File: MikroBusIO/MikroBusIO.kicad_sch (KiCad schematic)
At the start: 0 parts

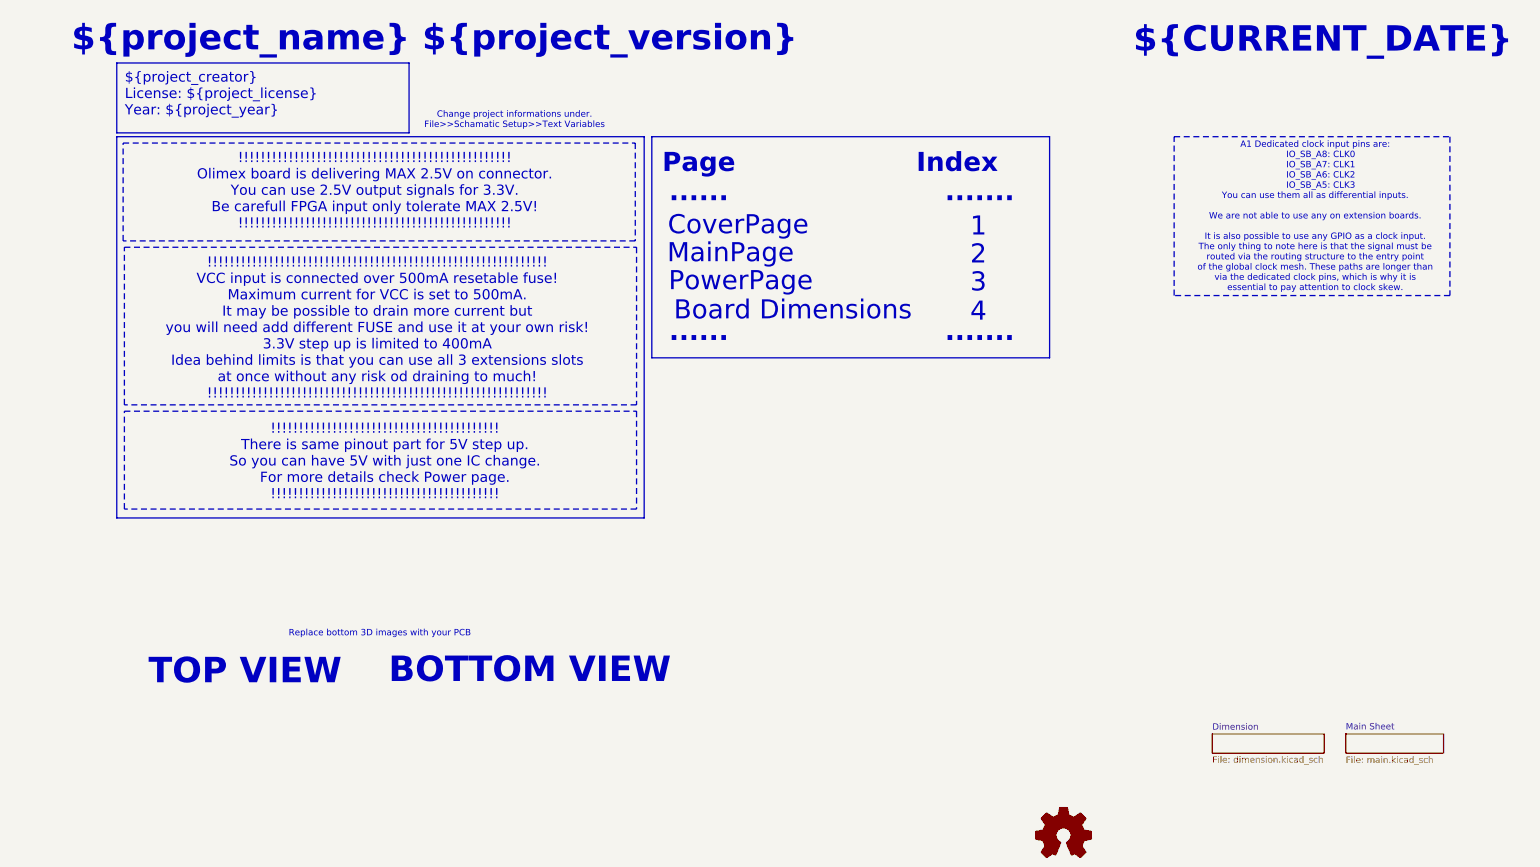
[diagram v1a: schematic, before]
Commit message: Cleanup MikroBus
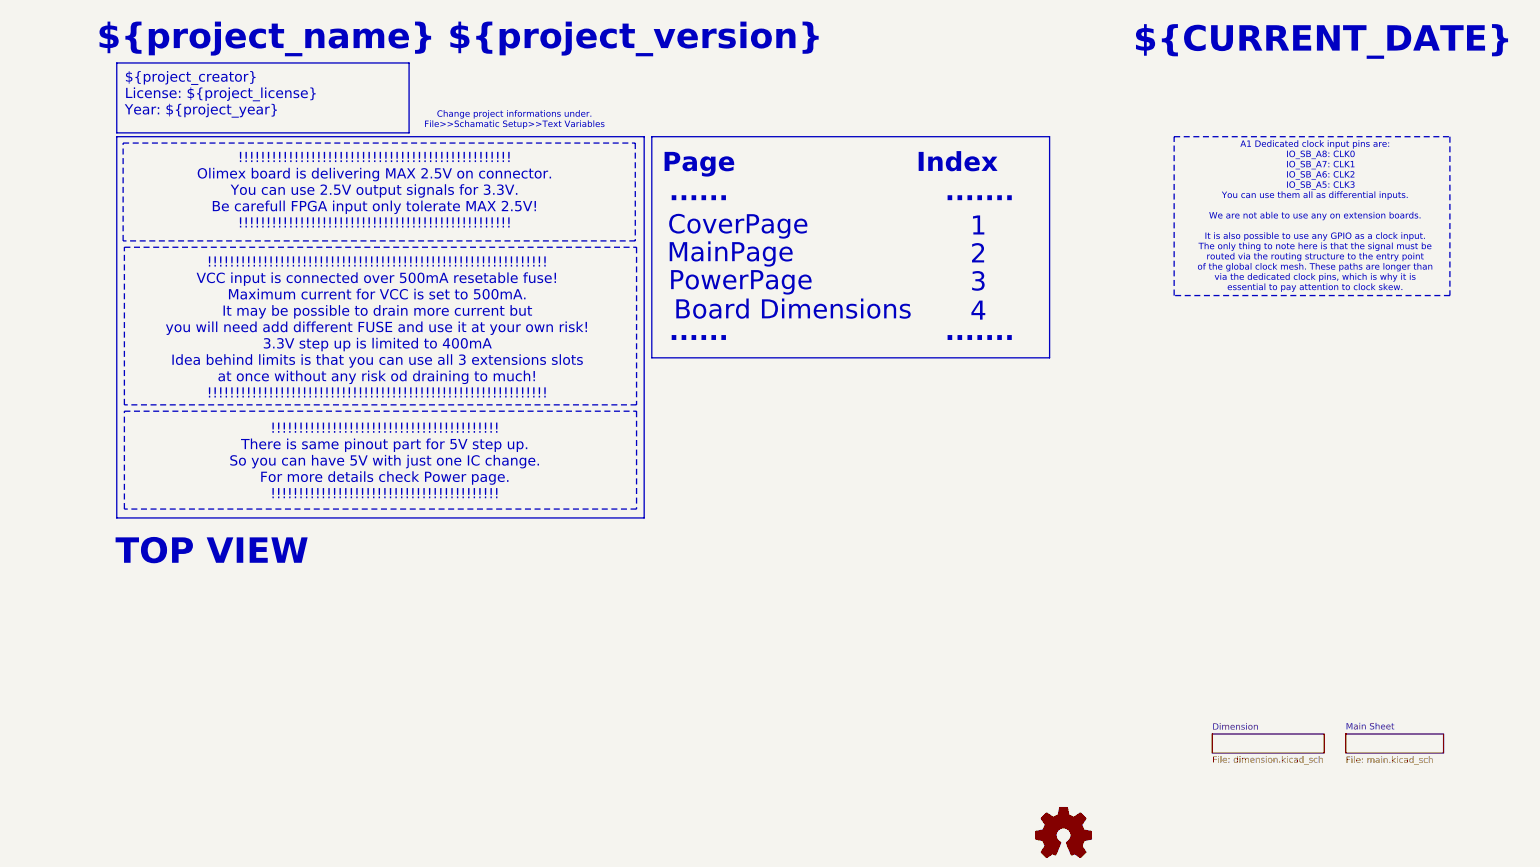
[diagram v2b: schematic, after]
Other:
- note removed: "BOTTOM VIEW"
- note removed: "Replace bottom 3D images with your PCB"
